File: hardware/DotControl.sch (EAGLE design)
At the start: 32 parts, among them CN1 1X4-BIG, J3 USB-MICROB, SW2 Previous, SW5 Previous, SW6 Next, SW8 Ok, U1 ATMEGA328P-MU-QFN32, U2 TMP102, U3 ATSHA204-TSU

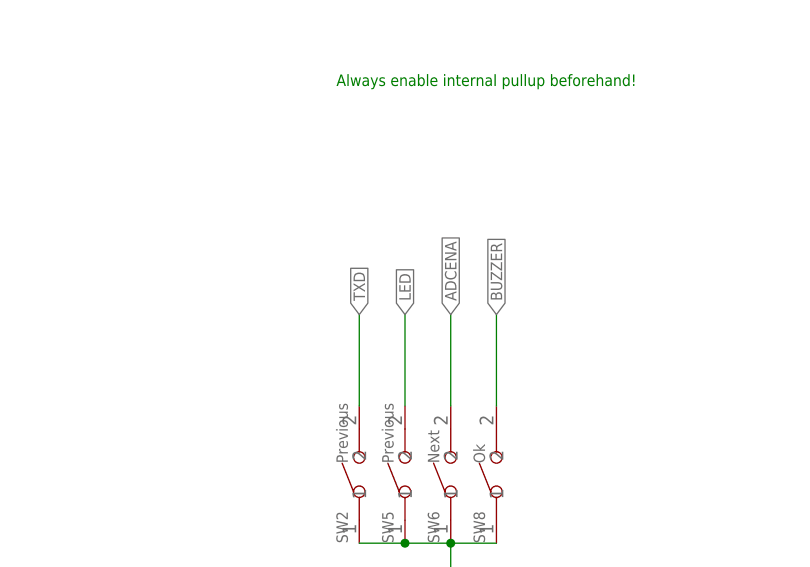
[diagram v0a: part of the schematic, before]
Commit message: Swap R with B @ pushbutton
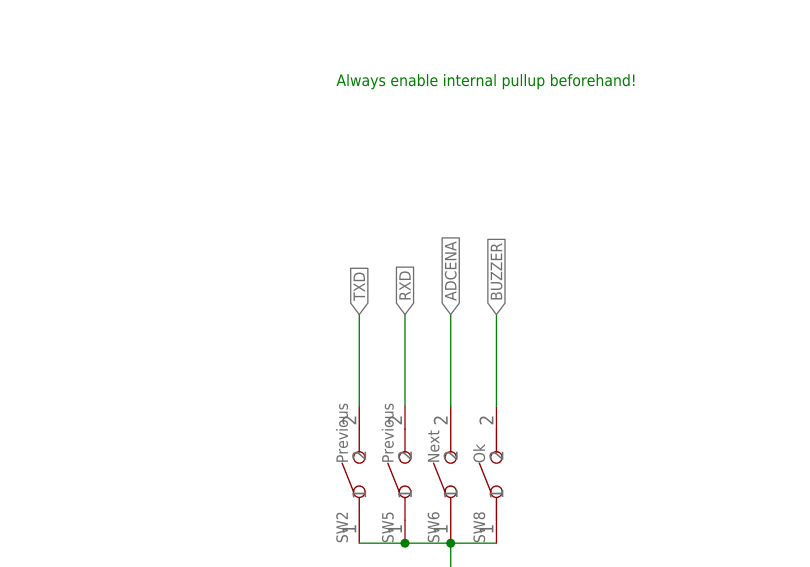
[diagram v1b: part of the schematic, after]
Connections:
- net LED: no longer SW5.2
- net RXD: now also SW5.2
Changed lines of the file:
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@@
 <pinref part="R2" gate="D" pin="1"/>
-</segment>
-<segment>
-<pinref part="SW5" gate="G$1" pin="2"/>
-<wire x1="88.9" y1="60.96" x2="88.9" y2="71.12" width="0.1524" layer="91"/>
-<label x="88.9" y="71.12" size="1.27" layer="95" rot="R90" xref="yes"/>
 </segment>
 </net>
@@
 <pinref part="R2" gate="C" pin="1"/>
 </segment>
+<segment>
+<pinref part="SW5" gate="G$1" pin="2"/>
+<wire x1="88.9" y1="60.96" x2="88.9" y2="71.12" width="0.1524" layer="91"/>
+<label x="88.9" y="71.12" size="1.27" layer="95" rot="R90" xref="yes"/>
+</segment>
 </net>

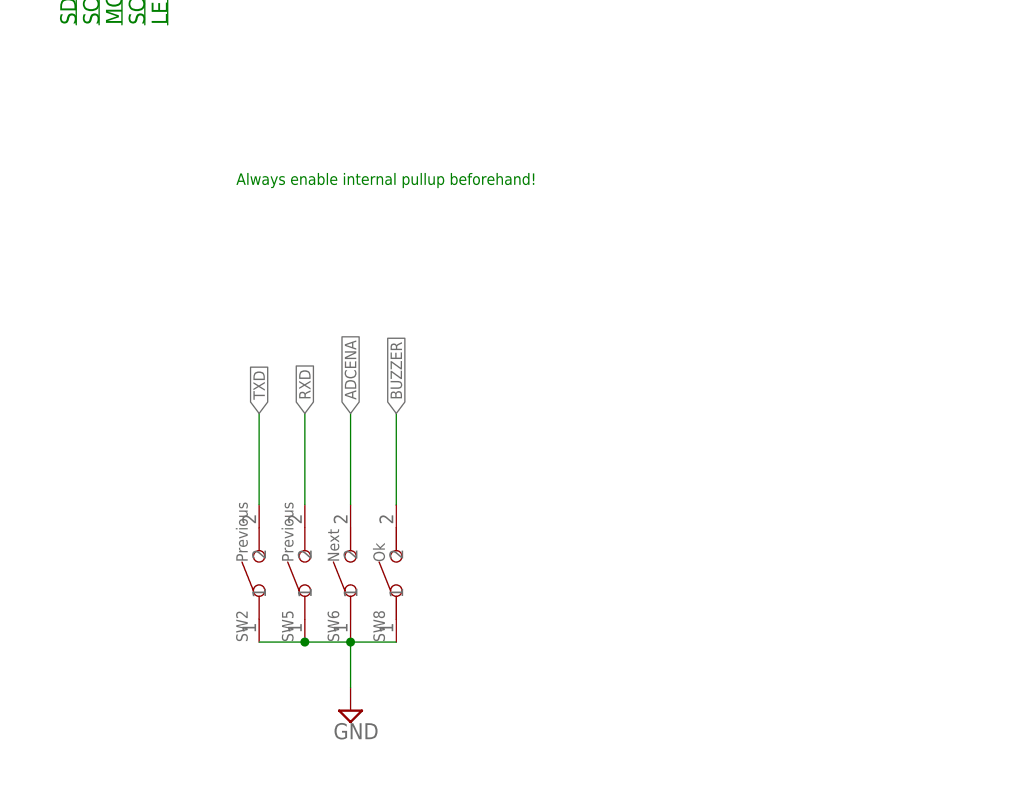
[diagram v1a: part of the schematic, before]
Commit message: Light RGB composite colors on push press
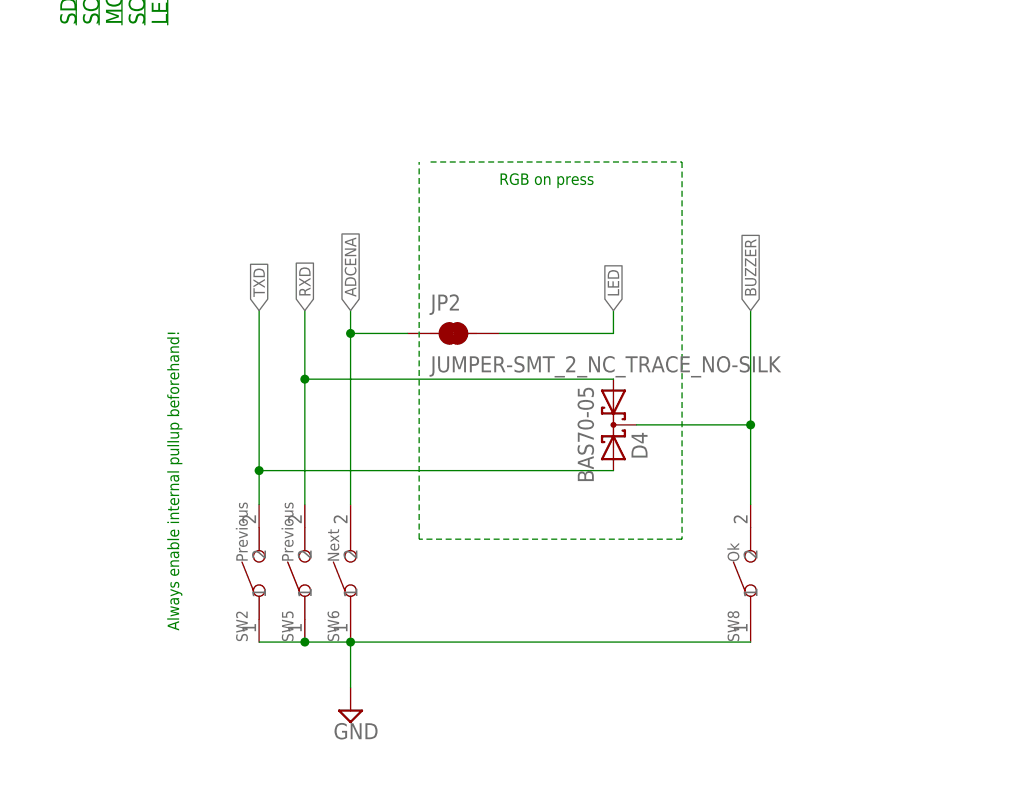
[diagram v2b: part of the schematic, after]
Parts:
- added D4: BAS70-05, diode:BAS70-05
- added JP2: JUMPER-SMT_2_NC_TRACE_NO-SILK, SparkFun-Jumpers:JUMPER-SMT_2_NC_TRACE_NO-SILK
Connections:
- net N$10 renamed BLUE
- net N$15 renamed RED
- net N$9 renamed GREEN
- net ADCENA: now also JP2.1
- net BUZZER: now also D4.C
- net LED: now also JP2.2
- net RXD: now also D4.A1
- net TXD: now also D4.A2
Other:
- note added: "RGB on press"
- moved on the sheet: SW8
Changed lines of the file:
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@@
 <setting verticaltext="up"/>
 </settings>
-<grid distance="0.1" unitdist="inch" unit="inch" style="lines" multiple="1" display="no" altdistance="0.01" altunitdist="inch" altunit="inch"/>
+<grid distance="0.05" unitdist="inch" unit="inch" style="lines" multiple="1" display="no" altdistance="0.01" altunitdist="inch" altunit="inch"/>
 <layers>
 <layer number="1" name="Top" color="4" fill="1" visible="no" active="no"/>
@@
 <part name="X1" library="adafruit" deviceset="ANTENNA_U.FL" device=""/>
 <part name="SUPPLY9" library="supply2" deviceset="GND" device=""/>
+<part name="D4" library="diode" deviceset="BAS70-05" device=""/>
+<part name="JP2" library="SparkFun-Jumpers" deviceset="JUMPER-SMT_2_NC_TRACE" device="_NO-SILK"/>
 </parts>
 <sheets>
@@
 <text x="180.34" y="259.08" size="1.27" layer="91" rot="R90">Green</text>
 <text x="189.738" y="259.08" size="1.27" layer="91">Red</text>
-<text x="81.28" y="96.52" size="1.27" layer="91">Always enable internal pullup beforehand!</text>
+<text x="74.93" y="46.99" size="1.27" layer="91" rot="R90">Always enable internal pullup beforehand!</text>
 <text x="238.76" y="91.44" size="1.778" layer="91">Temperature
 Humidity</text>
@@
 <text x="85.09" y="138.43" size="1.27" layer="91" rot="R90">LEDDisplay</text>
 <text x="208.28" y="71.12" size="3.81" layer="91">Authentification module</text>
+<text x="110.49" y="96.52" size="1.27" layer="91">RGB on press</text>
 </plain>
 <instances>
@@
 <instance part="SW6" gate="G$1" x="93.98" y="53.34" rot="R90"/>
 <instance part="SUPPLY13" gate="GND" x="93.98" y="38.1"/>
-<instance part="SW8" gate="G$1" x="99.06" y="53.34" rot="R90"/>
+<instance part="SW8" gate="G$1" x="138.43" y="53.34" rot="R90"/>
 <instance part="SUPPLY2" gate="GND" x="60.96" y="124.46"/>
 <instance part="U$2" gate="G$1" x="7.62" y="134.62"/>
@@
 <instance part="X1" gate="G$1" x="419.1" y="223.52" rot="R180"/>
 <instance part="SUPPLY9" gate="GND" x="424.18" y="226.06"/>
+<instance part="D4" gate="G$1" x="123.19" y="69.85" rot="R270"/>
+<instance part="JP2" gate="G$1" x="105.41" y="80.01"/>
 </instances>
 <busses>
@@
 <wire x1="88.9" y1="45.72" x2="93.98" y2="45.72" width="0.1524" layer="91"/>
 <pinref part="SW8" gate="G$1" pin="1"/>
-<wire x1="99.06" y1="45.72" x2="93.98" y2="45.72" width="0.1524" layer="91"/>
+<wire x1="138.43" y1="45.72" x2="93.98" y2="45.72" width="0.1524" layer="91"/>
 <junction x="93.98" y="45.72"/>
 <pinref part="SUPPLY13" gate="GND" pin="GND"/>
@@
 <pinref part="R2" gate="D" pin="1"/>
 </segment>
+<segment>
+<pinref part="JP2" gate="G$1" pin="2"/>
+<wire x1="110.49" y1="80.01" x2="123.19" y2="80.01" width="0.1524" layer="91"/>
+<wire x1="123.19" y1="80.01" x2="123.19" y2="82.55" width="0.1524" layer="91"/>
+<label x="123.19" y="82.55" size="1.27" layer="95" rot="R90" xref="yes"/>
+</segment>
 </net>
 <net name="LIGHT_SENSE" class="0">
@@
 <segment>
 <pinref part="SW6" gate="G$1" pin="2"/>
-<wire x1="93.98" y1="60.96" x2="93.98" y2="71.12" width="0.1524" layer="91"/>
-<label x="93.98" y="71.12" size="1.27" layer="95" rot="R90" xref="yes"/>
+<wire x1="93.98" y1="60.96" x2="93.98" y2="80.01" width="0.1524" layer="91"/>
+<label x="93.98" y="82.55" size="1.27" layer="95" rot="R90" xref="yes"/>
+<pinref part="JP2" gate="G$1" pin="1"/>
+<wire x1="93.98" y1="80.01" x2="93.98" y2="82.55" width="0.1524" layer="91"/>
+<wire x1="100.33" y1="80.01" x2="93.98" y2="80.01" width="0.1524" layer="91"/>
+<junction x="93.98" y="80.01"/>
 </segment>
 </net>
@@
 <segment>
 <pinref part="SW2" gate="G$1" pin="2"/>
-<wire x1="83.82" y1="60.96" x2="83.82" y2="71.12" width="0.1524" layer="91"/>
-<label x="83.82" y="71.12" size="1.27" layer="95" rot="R90" xref="yes"/>
+<wire x1="83.82" y1="60.96" x2="83.82" y2="64.77" width="0.1524" layer="91"/>
+<label x="83.82" y="82.55" size="1.27" layer="95" rot="R90" xref="yes"/>
+<pinref part="D4" gate="G$1" pin="A2"/>
+<wire x1="83.82" y1="64.77" x2="83.82" y2="82.55" width="0.1524" layer="91"/>
+<wire x1="123.19" y1="64.77" x2="83.82" y2="64.77" width="0.1524" layer="91"/>
+<junction x="83.82" y="64.77"/>
 </segment>
 </net>
@@
 <segment>
 <pinref part="SW5" gate="G$1" pin="2"/>
-<wire x1="88.9" y1="60.96" x2="88.9" y2="71.12" width="0.1524" layer="91"/>
-<label x="88.9" y="71.12" size="1.27" layer="95" rot="R90" xref="yes"/>
+<wire x1="88.9" y1="60.96" x2="88.9" y2="74.93" width="0.1524" layer="91"/>
+<label x="88.9" y="82.55" size="1.27" layer="95" rot="R90" xref="yes"/>
+<pinref part="D4" gate="G$1" pin="A1"/>
+<wire x1="88.9" y1="74.93" x2="88.9" y2="82.55" width="0.1524" layer="91"/>
+<wire x1="123.19" y1="74.93" x2="88.9" y2="74.93" width="0.1524" layer="91"/>
+<junction x="88.9" y="74.93"/>
 </segment>
 </net>
@@
 <segment>
 <pinref part="SW8" gate="G$1" pin="2"/>
-<wire x1="99.06" y1="60.96" x2="99.06" y2="71.12" width="0.1524" layer="91"/>
-<label x="99.06" y="71.12" size="1.27" layer="95" rot="R90" xref="yes"/>
+<wire x1="138.43" y1="60.96" x2="138.43" y2="69.85" width="0.1524" layer="91"/>
+<label x="138.43" y="82.55" size="1.27" layer="95" rot="R90" xref="yes"/>
+<pinref part="D4" gate="G$1" pin="C"/>
+<wire x1="138.43" y1="69.85" x2="138.43" y2="82.55" width="0.1524" layer="91"/>
+<wire x1="125.73" y1="69.85" x2="138.43" y2="69.85" width="0.1524" layer="91"/>
+<junction x="138.43" y="69.85"/>
 </segment>
 </net>
@@
 </segment>
 </net>
-<net name="N$9" class="0">
+<net name="GREEN" class="0">
 <segment>
 <pinref part="LED1" gate="G$1" pin="CBLUE"/>
@@
 </segment>
 </net>
-<net name="N$15" class="0">
+<net name="RED" class="0">
 <segment>
 <pinref part="LED1" gate="G$1" pin="CGREEN"/>
@@
 </segment>
 </net>
-<net name="N$10" class="0">
+<net name="BLUE" class="0">
 <segment>
 <pinref part="LED1" gate="G$1" pin="CRED"/>
@@
 </segment>
 </net>
+<net name="N$9" class="0">
+<segment>
+<wire x1="102.87" y1="99.06" x2="130.81" y2="99.06" width="0.1524" layer="91" style="shortdash"/>
+<wire x1="130.81" y1="99.06" x2="130.81" y2="57.15" width="0.1524" layer="91" style="shortdash"/>
+<wire x1="130.81" y1="57.15" x2="101.6" y2="57.15" width="0.1524" layer="91" style="shortdash"/>
+<wire x1="101.6" y1="57.15" x2="101.6" y2="99.06" width="0.1524" layer="91" style="shortdash"/>
+</segment>
+</net>

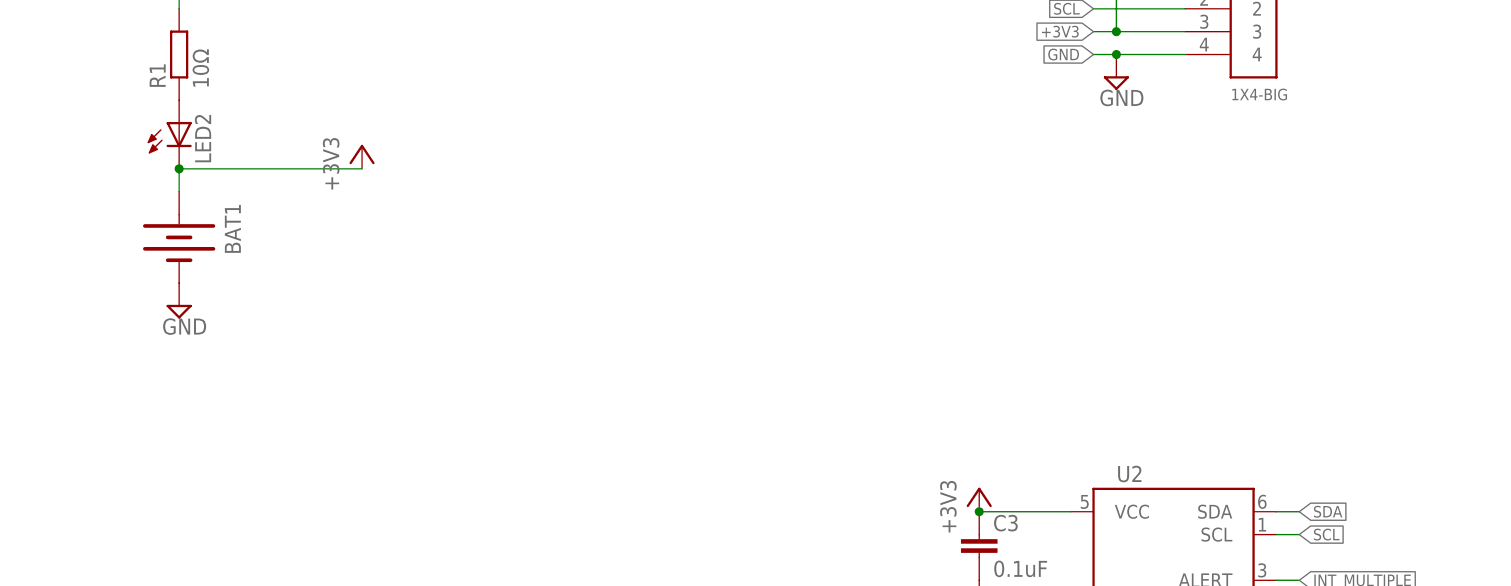
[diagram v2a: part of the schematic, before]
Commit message: Add Si7021 temp sensor
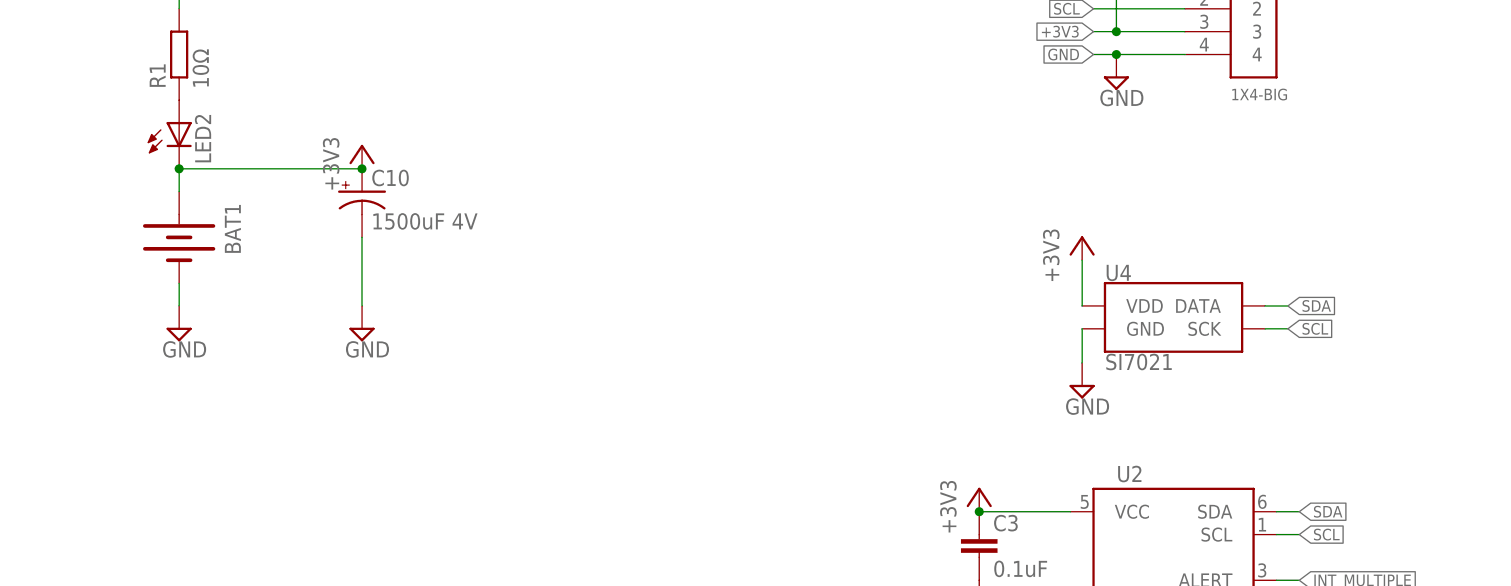
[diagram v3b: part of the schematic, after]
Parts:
- added C10: 1500uF 4V, adafruit:CPOL-USCT7343
- added U4: SI7021, SparkFun-Sensors:SI7021
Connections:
- net +3V3: now also C10.+, U4.VDD
- net GND: now also C10.-, U4.GND
- net SCL: now also U4.SCK
- net SDA: now also U4.DATA
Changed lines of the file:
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@@
 <part name="D4" library="diode" deviceset="BAS70-05" device=""/>
 <part name="JP2" library="SparkFun-Jumpers" deviceset="JUMPER-SMT_2_NC_TRACE" device="_NO-SILK"/>
+<part name="U4" library="SparkFun-Sensors" deviceset="SI7021" device=""/>
+<part name="+3V12" library="supply1" deviceset="+3V3" device=""/>
+<part name="SUPPLY11" library="supply2" deviceset="GND" device=""/>
+<part name="C10" library="adafruit" deviceset="CPOL-US" device="CT7343" value="1500uF 4V"/>
+<part name="SUPPLY16" library="supply2" deviceset="GND" device=""/>
 </parts>
 <sheets>
@@
 <instance part="SW2" gate="G$1" x="83.82" y="53.34" rot="R90"/>
 <instance part="JP1" gate="G$1" x="66.04" y="127" rot="MR270"/>
-<instance part="SUPPLY8" gate="GND" x="114.3" y="132.08"/>
+<instance part="SUPPLY8" gate="GND" x="114.3" y="129.54"/>
 <instance part="BAT1" gate="G$1" x="114.3" y="139.7" rot="R270"/>
 <instance part="+3V14" gate="G$1" x="177.8" y="289.56"/>
@@
 <instance part="D4" gate="G$1" x="123.19" y="69.85" rot="R270"/>
 <instance part="JP2" gate="G$1" x="105.41" y="80.01"/>
+<instance part="U4" gate="G$1" x="224.79" y="129.54"/>
+<instance part="+3V12" gate="G$1" x="214.63" y="139.7"/>
+<instance part="SUPPLY11" gate="GND" x="214.63" y="123.19"/>
+<instance part="C10" gate="G$1" x="134.62" y="144.78"/>
+<instance part="SUPPLY16" gate="GND" x="134.62" y="129.54"/>
 </instances>
 <busses>
@@
 <pinref part="SUPPLY8" gate="GND" pin="GND"/>
 <pinref part="BAT1" gate="G$1" pin="-"/>
+<wire x1="114.3" y1="132.08" x2="114.3" y2="134.62" width="0.1524" layer="91"/>
 </segment>
 <segment>
@@
 <junction x="424.18" y="228.6"/>
 </segment>
+<segment>
+<pinref part="U4" gate="G$1" pin="GND"/>
+<pinref part="SUPPLY11" gate="GND" pin="GND"/>
+<wire x1="214.63" y1="129.54" x2="214.63" y2="125.73" width="0.1524" layer="91"/>
+</segment>
+<segment>
+<pinref part="C10" gate="G$1" pin="-"/>
+<pinref part="SUPPLY16" gate="GND" pin="GND"/>
+<wire x1="134.62" y1="139.7" x2="134.62" y2="132.08" width="0.1524" layer="91"/>
+</segment>
 </net>
 <net name="SCK" class="0">
@@
 <label x="238.76" y="109.22" size="1.27" layer="95" xref="yes"/>
 </segment>
+<segment>
+<pinref part="U4" gate="G$1" pin="DATA"/>
+<wire x1="234.95" y1="132.08" x2="237.49" y2="132.08" width="0.1524" layer="91"/>
+<label x="237.49" y="132.08" size="1.27" layer="95" xref="yes"/>
+</segment>
 </net>
 <net name="SCL" class="0">
@@
 <wire x1="236.22" y1="106.68" x2="238.76" y2="106.68" width="0.1524" layer="91"/>
 <label x="238.76" y="106.68" size="1.27" layer="95" xref="yes"/>
+</segment>
+<segment>
+<pinref part="U4" gate="G$1" pin="SCK"/>
+<wire x1="234.95" y1="129.54" x2="237.49" y2="129.54" width="0.1524" layer="91"/>
+<label x="237.49" y="129.54" size="1.27" layer="95" xref="yes"/>
 </segment>
 </net>
@@
 <wire x1="134.62" y1="147.32" x2="114.3" y2="147.32" width="0.1524" layer="91"/>
 <junction x="114.3" y="147.32"/>
-</segment>
-</net>
+<pinref part="C10" gate="G$1" pin="+"/>
+<junction x="134.62" y="147.32"/>
+</segment>
+<segment>
+<pinref part="+3V12" gate="G$1" pin="+3V3"/>
+<pinref part="U4" gate="G$1" pin="VDD"/>
+<wire x1="214.63" y1="137.16" x2="214.63" y2="132.08" width="0.1524" layer="91"/>
+</segment>
+</net>
